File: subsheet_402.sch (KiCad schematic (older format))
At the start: 39 parts, among them J400 DIN-13S — Video Port, Q400 2N3904, Q401 2N3904, Q402 2N3904, Q403 2N3904, U405 74S257_PHY

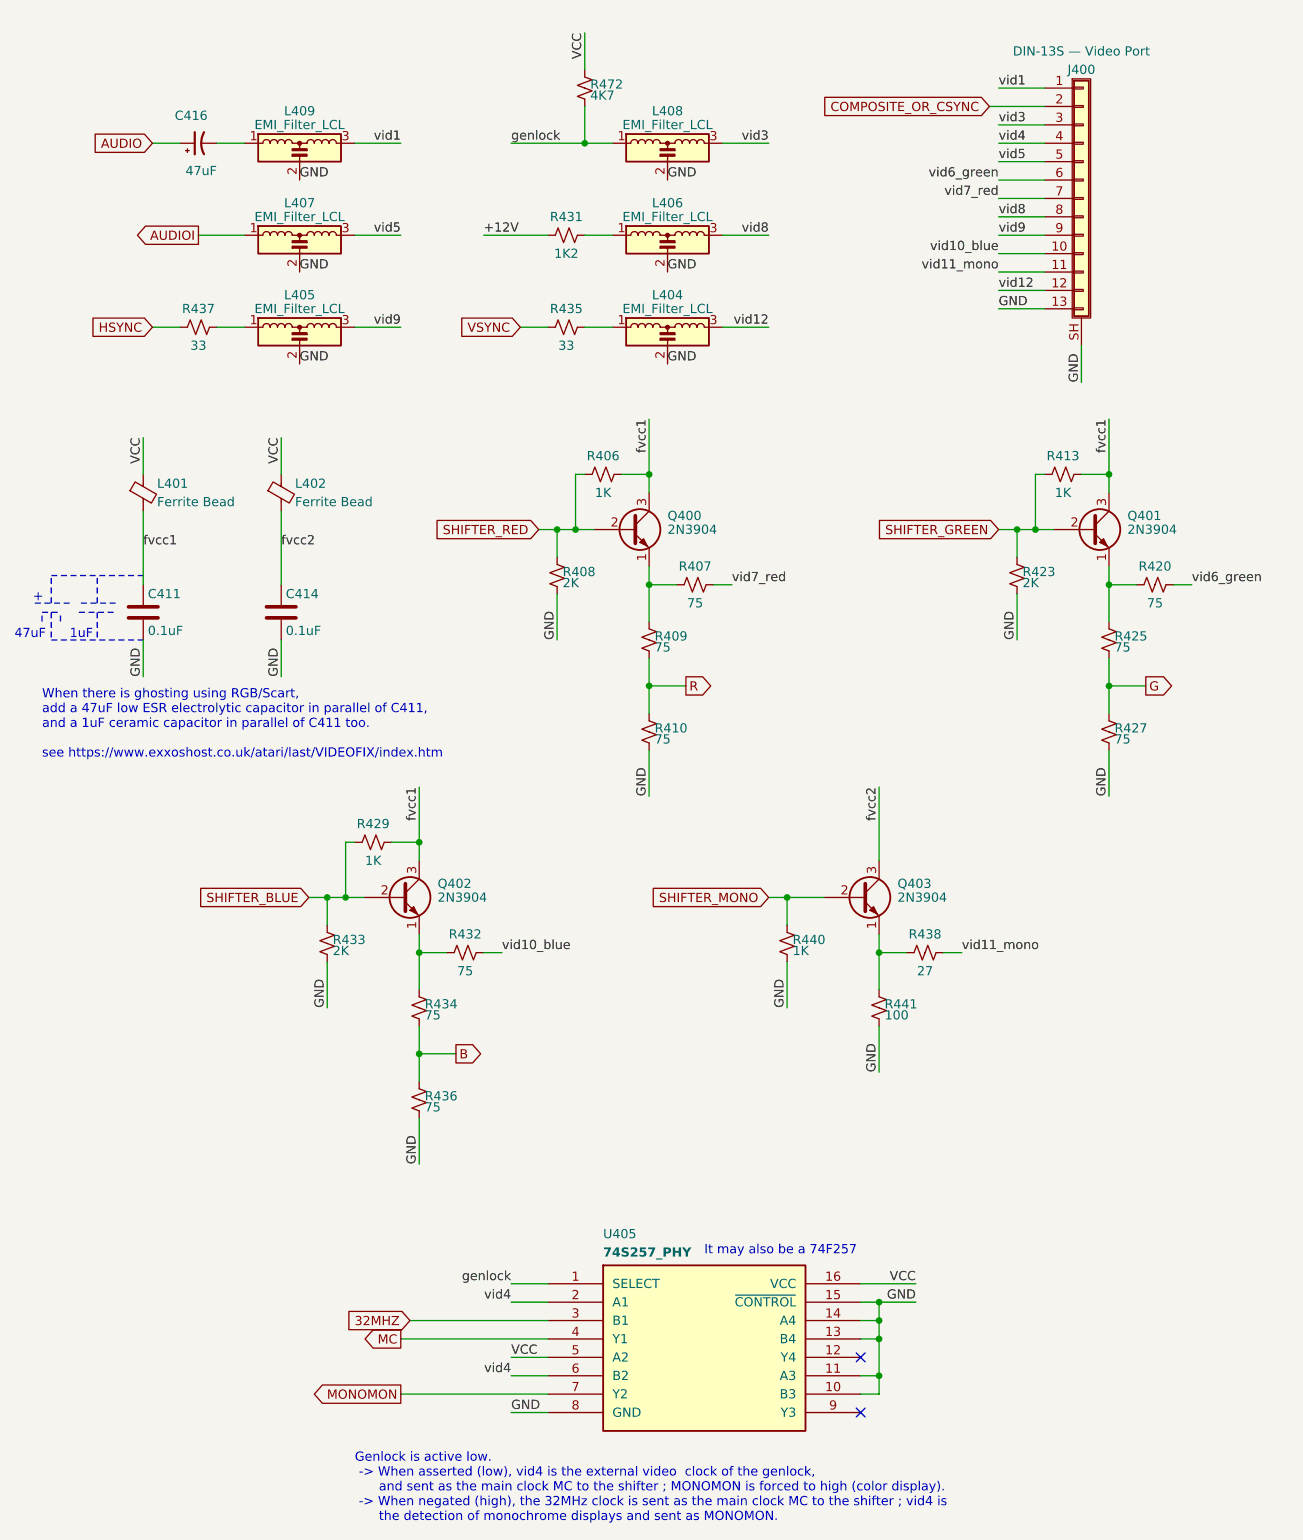
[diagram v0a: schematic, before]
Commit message: Delete circuitry related to PAL/NTSC and modulator
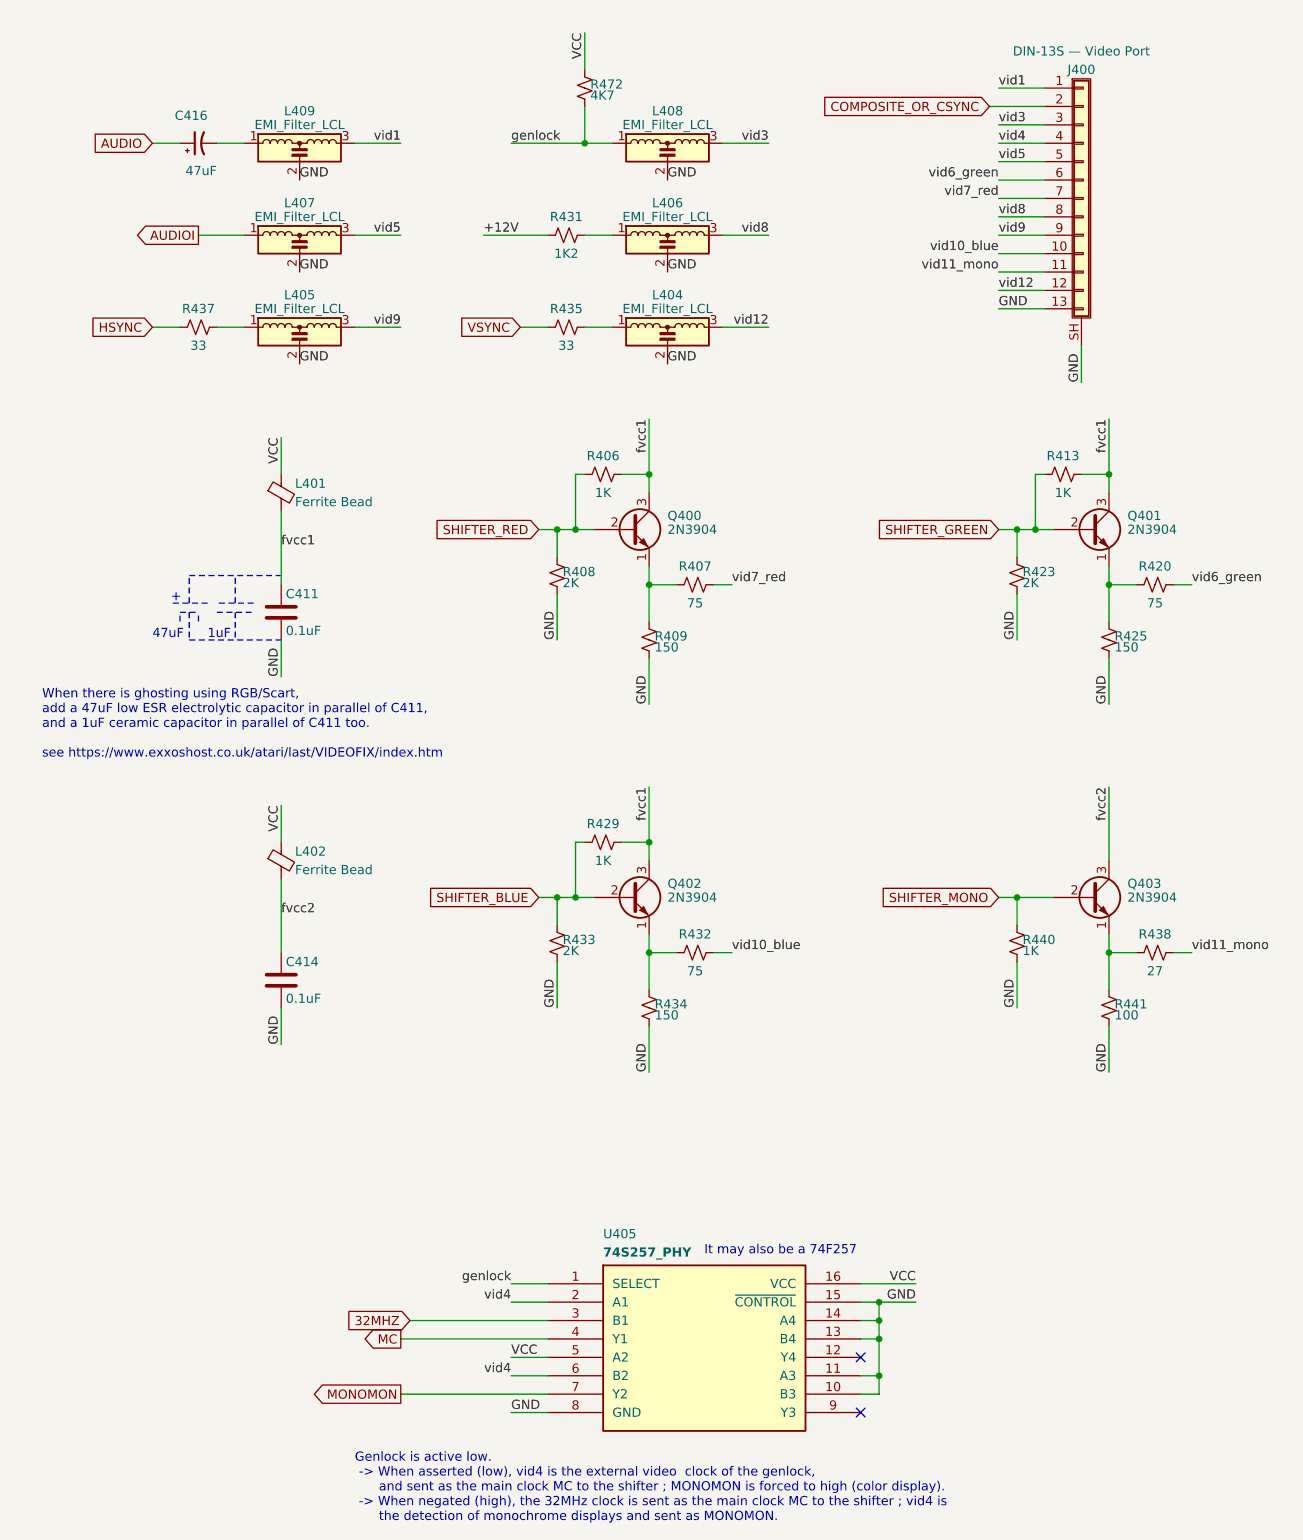
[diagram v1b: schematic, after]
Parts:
- removed R410, R427, R436: 75, commons_passives_THT:Passive_THT_resistor_W2.54mm_L12.70mm, symbol Device:R_Small_US
- R409, R425, R434: value 75 -> 150
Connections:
- net B is gone; now on net GND: R434.2
- net G is gone; now on net GND: R425.2
- net R is gone; now on net GND: R409.2
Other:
- moved on the sheet: C411, C414, L401, L402, Q402, Q403, R429, R432, R433, R434, R438, R440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

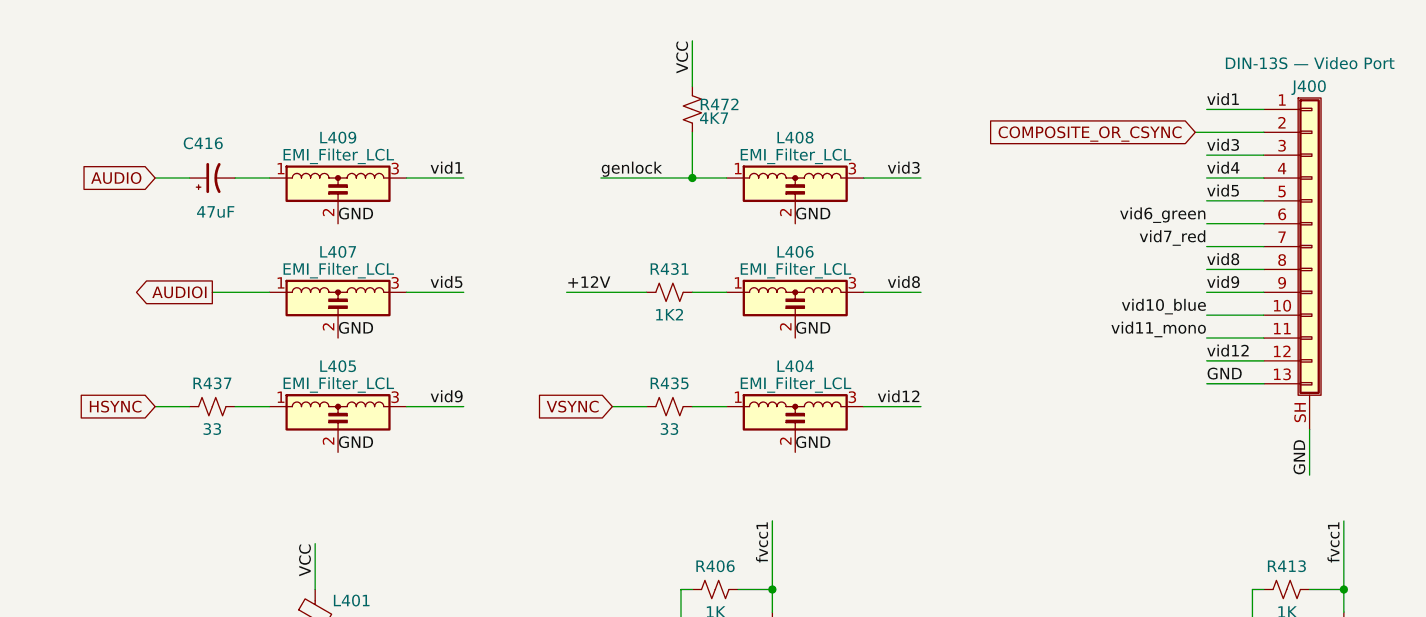
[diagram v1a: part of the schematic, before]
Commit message: Removed T-filters
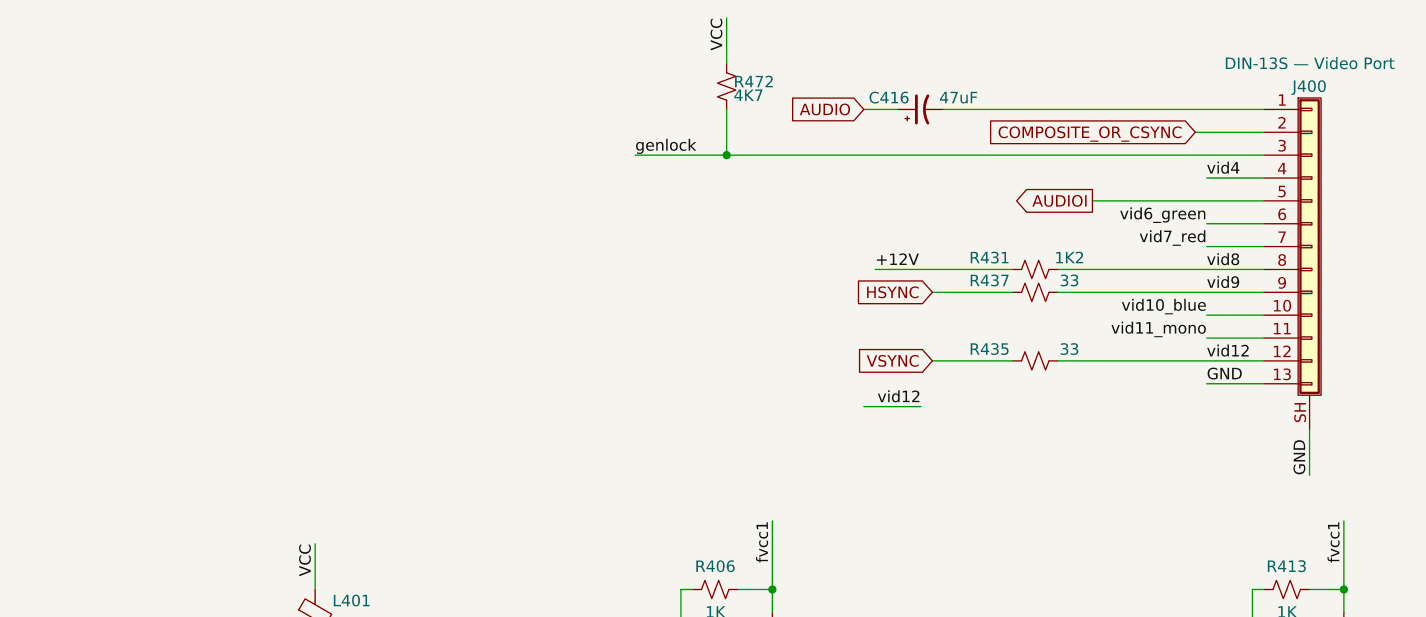
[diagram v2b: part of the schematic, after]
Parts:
- removed L404, L405, L406, L407, L408, L409: EMI_Filter_LCL, commons_passives_THT:Passive_THT_EMI_filter_W5.08mm_L7.62mm, symbol Device:EMI_Filter_LCL
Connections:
- net vid1 is gone; now on an unnamed net: J400.1 (Pin_1)
- net vid3 is gone; now on net genlock: J400.3 (Pin_3)
- net vid5 is gone; now on net AUDIOI: J400.5 (Pin_5)
- net vid12: now also R435.1
- net vid8: now also R431.1
- net vid9: now also R437.1
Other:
- moved on the sheet: C416, R431, R435, R437, R472

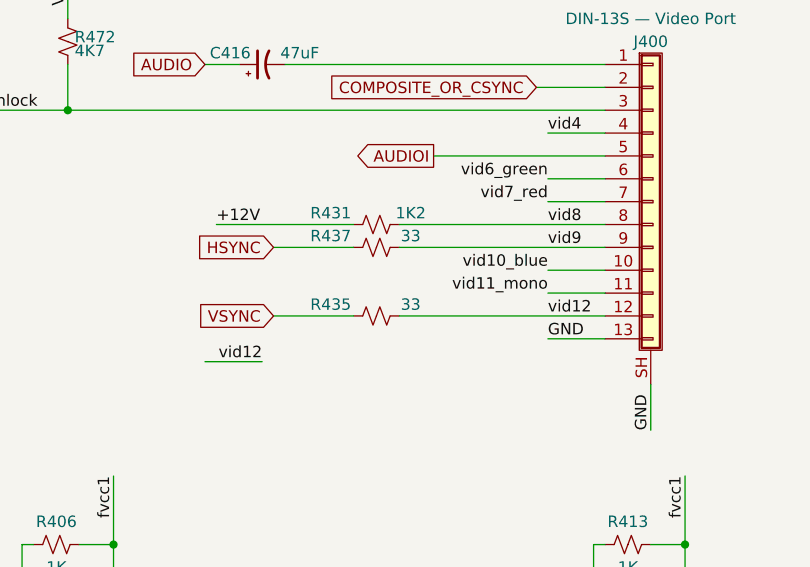
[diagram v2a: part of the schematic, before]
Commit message: Resolves #1 : Use 4-resistor packs wherever it is possible
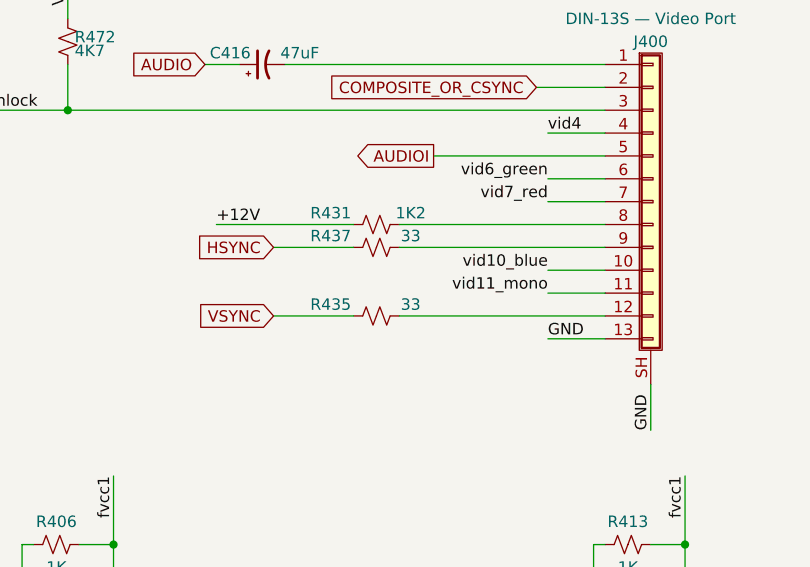
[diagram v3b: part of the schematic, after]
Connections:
- net vid12: no longer names the net of J400.12 (Pin_12), R435.1
- net vid8: no longer names the net of J400.8 (Pin_8), R431.1
- net vid9: no longer names the net of J400.9 (Pin_9), R437.1
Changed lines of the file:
@@
 Text Label 5900 1900 2    50   ~ 0
 vid7_red
-Text Label 5900 2000 0    50   ~ 0
-vid8
-Text Label 5900 2100 0    50   ~ 0
-vid9
 Text Label 5900 2200 2    50   ~ 0
 vid10_blue
@@
 	0    1    1    0
 $EndComp
-Wire Wire Line
-	4400 2600 4650 2600
 $Comp
 L Device:R_Small_US R?
@@
 	0    1    1    0
 $EndComp
-Text Label 4650 2600 2    50   ~ 0
-vid12
 Text GLabel 4700 2400 0    50   Input ~ 0
 VSYNC
@@
 Wire Wire Line
 	3800 900  3800 1100
-Text Label 5900 2400 0    50   ~ 0
-vid12
 $Comp
 L 74x257:74S257_PHY U405

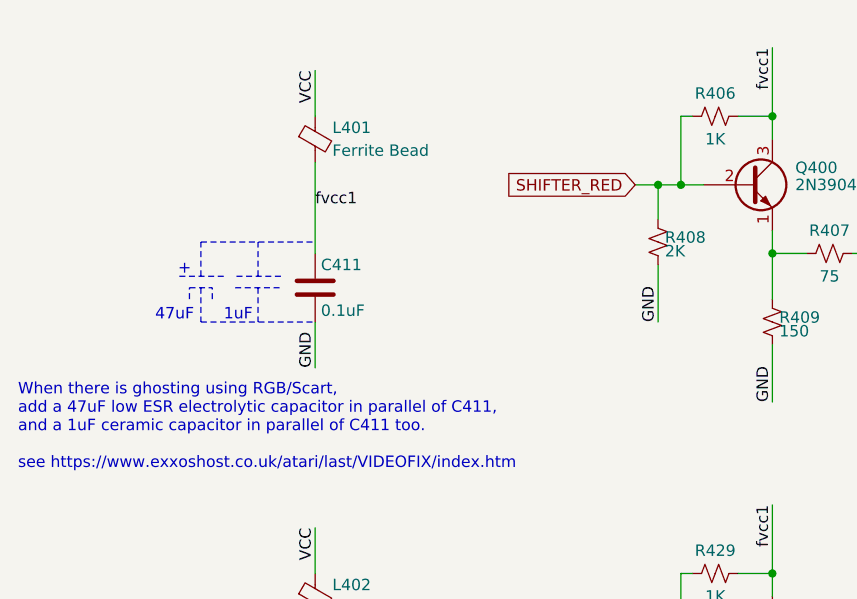
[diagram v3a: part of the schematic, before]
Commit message: Resolves #5 : Apply the fix for the video ghosting
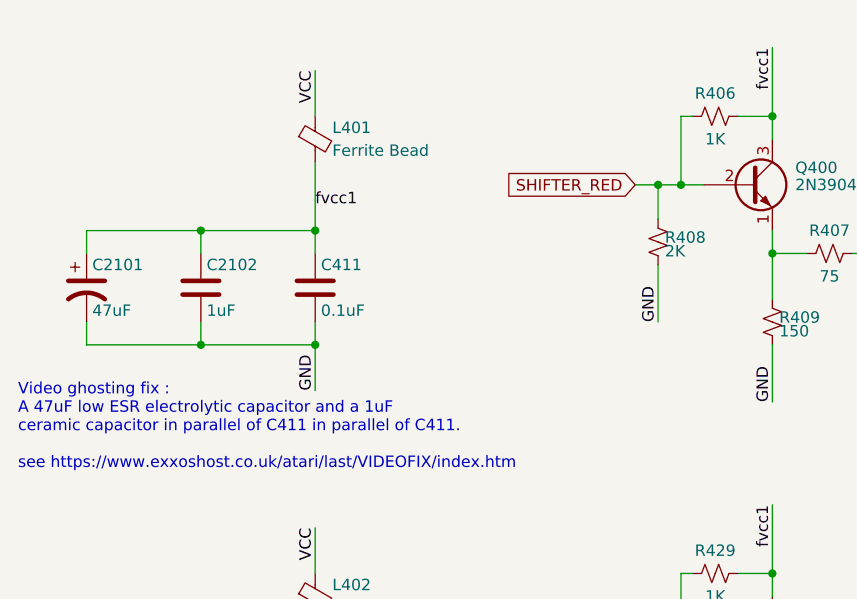
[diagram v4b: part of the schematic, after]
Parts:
- added C2101: 47uF, commons_passives_THT:Passive_THT_capacitor_polarized_W6.35mm_L20.32mm, symbol Device:CP1
- added C2102: 1uF, commons_passives_THT:Passive_THT_capacitor_mlcc_W2.54mm_L10.16mm, symbol Device:C
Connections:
- net GND: now also C2101.2, C2102.2
- net fvcc1: now also C2101.1, C2102.1
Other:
- note added: "Video ghosting fix : \nA 47uF low ESR electrolytic capacitor and a 1uF\nceramic capacitor in parallel of C411 in parallel of C411.\n\nsee https://www.exxoshost.co.uk/atari/last/VIDEOFIX/index.htm\n"
- note removed: "+"
- note removed: "1uF"
- note removed: "47uF"
- note removed: "When there is ghosting using RGB/Scart, \nadd a 47uF low ESR electrolytic capacitor in parallel of C411, \nand a 1uF ceramic capacitor in parallel of C411 too.\n\nsee https://www.exxoshost.co.uk/atari/last/VIDEOFIX/index.htm\n"
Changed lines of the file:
@@
 	1    0    0    -1
 $EndComp
-Text Label 2000 4500 1    50   ~ 0
-GND
-Wire Wire Line
-	2000 4300 2000 4500
+Text Label 2000 4600 1    50   ~ 0
+GND
+Wire Wire Line
+	2000 4400 2000 4600
 Text Label 2000 3800 0    50   ~ 0
 fvcc1
@@
 VCC
 Wire Wire Line
-	2000 3600 2000 4000
+	2000 3600 2000 3900
 Wire Wire Line
 	2000 5600 2000 6000
@@
 	6350 2900 6350 2700
 Text Notes 700  4950 0    50   ~ 0
-When there is ghosting using RGB/Scart, \nadd a 47uF low ESR electrolytic capacitor in parallel of C411, \nand a 1uF ceramic capacitor in parallel of C411 too.\n\nsee https://www.exxoshost.co.uk/atari/last/VIDEOFIX/index.htm\n
-Wire Notes Line
-	1850 4100 1650 4100
-Wire Notes Line
-	1650 4150 1850 4150
-Wire Notes Line
-	1600 4100 1400 4100
-Wire Notes Line
-	1500 4150 1500 4300
-Wire Notes Line
-	1500 4300 2000 4300
-Wire Notes Line
-	1750 4150 1750 4300
-Wire Notes Line
-	1500 4100 1500 3950
-Wire Notes Line
-	1500 3950 2000 3950
-Wire Notes Line
-	1750 4100 1750 3950
-Wire Notes Line
-	1450 4200 1450 4150
-Wire Notes Line
-	1550 4200 1550 4150
-Wire Notes Line
-	1450 4150 1550 4150
-Text Notes 1300 4300 0    50   ~ 0
-47uF
-Text Notes 1400 4100 0    50   ~ 0
-+
-Text Notes 1600 4300 0    50   ~ 0
-1uF
+Video ghosting fix :  \nA 47uF low ESR electrolytic capacitor and a 1uF\nceramic capacitor in parallel of C411 in parallel of C411.\n\nsee https://www.exxoshost.co.uk/atari/last/VIDEOFIX/index.htm\n
 Wire Wire Line
 	3800 1500 6150 1500
@@
 Wire Wire Line
 	5250 2400 6150 2400
+$Comp
+L Device:C C?
+U 1 1 61CE7083
+P 1500 4150
+AR Path="/60786F27/6078774E/61CE7083" Ref="C?"  Part="1"
+AR Path="/60786F27/607875AF/61CE7083" Ref="C?"  Part="1"
+AR Path="/6089D0BA/61CE7083" Ref="C?"  Part="1"
+AR Path="/608A2359/61CE7083" Ref="C?"  Part="1"
+AR Path="/60A1445F/61CE7083" Ref="C?"  Part="1"
+AR Path="/60A73CDE/61CE7083" Ref="C?"  Part="1"
+AR Path="/60AD8617/61CE7083" Ref="C?"  Part="1"
+AR Path="/60AD332C/61CE7083" Ref="C?"  Part="1"
+AR Path="/60AD33B6/61CE7083" Ref="C?"  Part="1"
+AR Path="/60B3D9E3/61CE7083" Ref="C2102"  Part="1"
+F 0 "C2102" H 1525 4250 50  0000 L CNN
+F 1 "1uF" H 1525 4050 50  0000 L CNN
+F 2 "commons_passives_THT:Passive_THT_capacitor_mlcc_W2.54mm_L10.16mm" H 1538 4000 50  0001 C CNN
+F 3 "~" H 1500 4150 50  0001 C CNN
+	1    1500 4150
+	1    0    0    -1
+$EndComp
+$Comp
+L Device:CP1 C?
+U 1 1 61CEA8C5
+P 1000 4150
+AR Path="/6089D0C2/61CEA8C5" Ref="C?"  Part="1"
+AR Path="/60B3D9E3/61CEA8C5" Ref="C2101"  Part="1"
+F 0 "C2101" H 1025 4250 50  0000 L CNN
+F 1 "47uF" H 1025 4050 50  0000 L CNN
+F 2 "commons_passives_THT:Passive_THT_capacitor_polarized_W6.35mm_L20.32mm" H 1000 4150 50  0001 C CNN
+F 3 "~" H 1000 4150 50  0001 C CNN
+	1    1000 4150
+	1    0    0    -1
+$EndComp
+Wire Wire Line
+	2000 4400 1500 4400
+Wire Wire Line
+	1000 4400 1000 4300
+Wire Wire Line
+	1000 4000 1000 3900
+Wire Wire Line
+	1000 3900 1500 3900
+Connection ~ 2000 3900
+Wire Wire Line
+	2000 3900 2000 4000
+Wire Wire Line
+	1500 4000 1500 3900
+Connection ~ 1500 3900
+Wire Wire Line
+	1500 3900 2000 3900
+Wire Wire Line
+	1500 4300 1500 4400
+Connection ~ 1500 4400
+Wire Wire Line
+	1500 4400 1000 4400
+Wire Wire Line
+	2000 4400 2000 4300
+Connection ~ 2000 4400
 $EndSCHEMATC
